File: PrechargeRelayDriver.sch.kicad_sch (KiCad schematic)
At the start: 7 parts, among them K4 G2RL-2A, K7 G7L-2A-X-SI_DC12, Q3 DMN61D8LQ

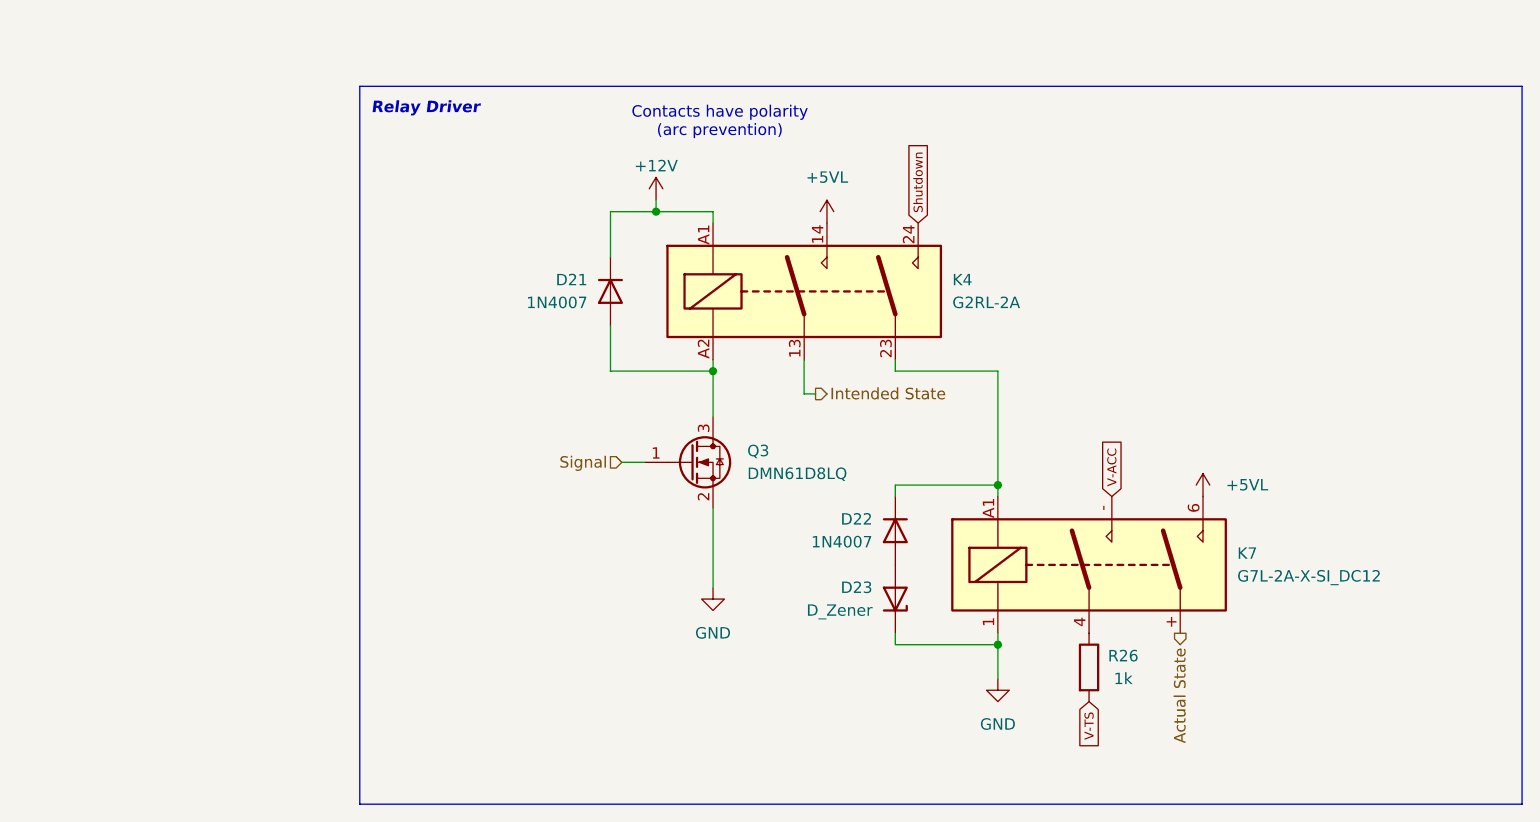
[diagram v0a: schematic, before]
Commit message: Updated to single pole relay, removed relay drivers
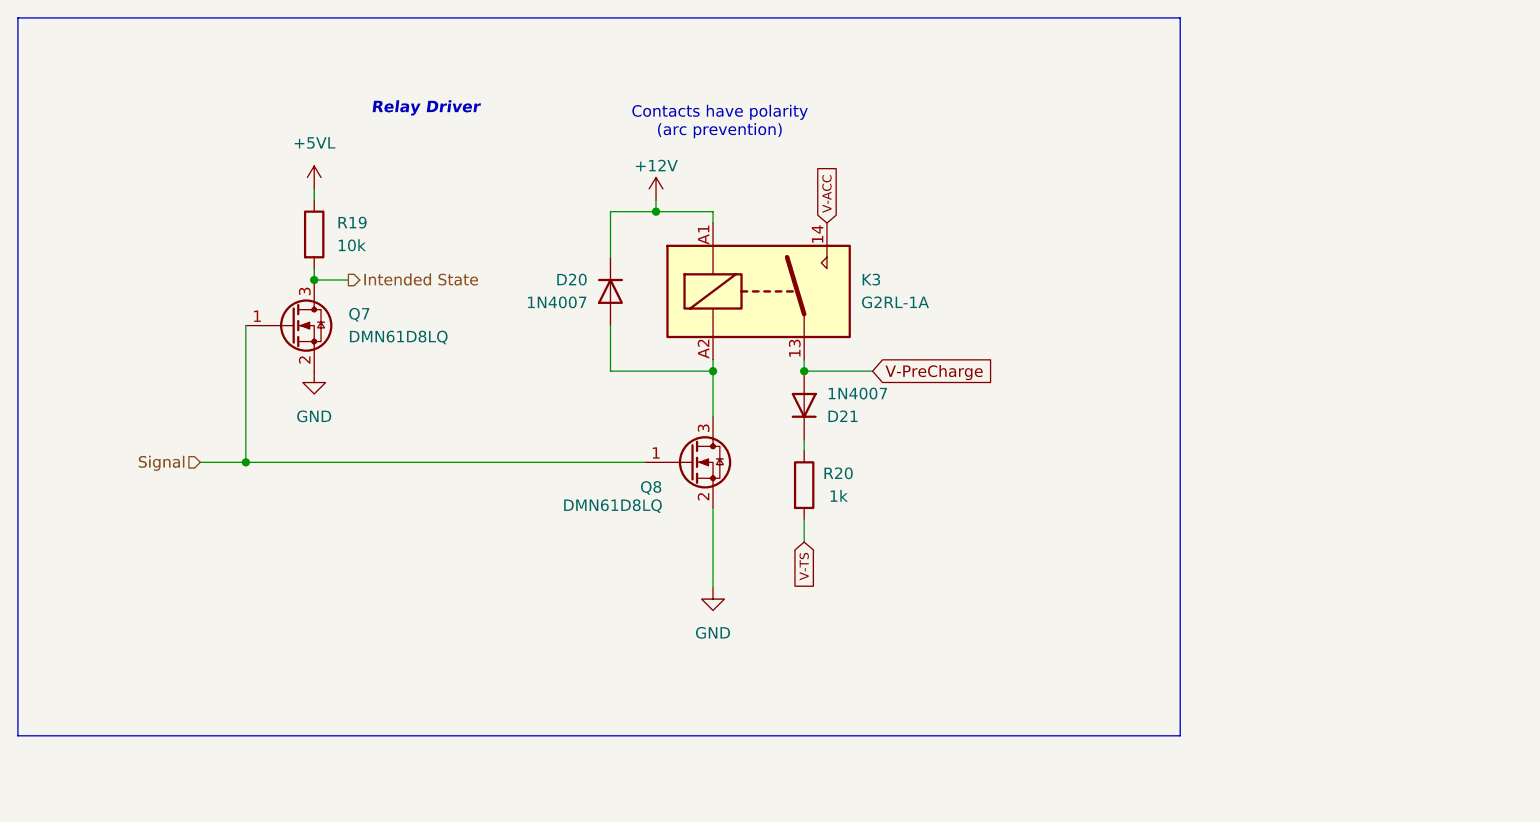
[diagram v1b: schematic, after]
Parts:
- removed D22: 1N4007, Diode_SMD:D_SMA, symbol Diode:1N4007
- removed D23: D_Zener, symbol Device:D_Zener
- removed K4: G2RL-2A, Relay_THT:Relay_DPST_Omron_G2RL-2A, symbol Relay:G2RL-2A
- removed K7: G7L-2A-X-SI_DC12, MyLibrary:G7L2AXSIDC12, symbol Relay:G2RL-2A
- added D21: 1N4007, Diode_SMD:D_SMA, symbol Diode:1N4007
- added K3: G2RL-1A, Relay_THT:Relay_SPST_Omron_G2RL-1A, symbol Relay:G2RL-1A
- added Q7: DMN61D8LQ, Package_TO_SOT_SMD:SOT-23, symbol Transistor_FET:DMN61D8LQ
- added R19: 10k, Resistor_SMD:R_0603_1608Metric, symbol Device:R
- renumbered D21 to D20, Q3 to Q8, R26 to R20
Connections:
- net +12V: now also K3.A1
- net +5VL: now also R19.1
- net GND: now also Q7.2 (S)
- net Intended State: now also Q7.3 (D), R19.2
- net Signal: now also Q7.1 (G)
- net V-ACC: now also K3.14
- net at D20.2 (A), Q8.3 (D): now also K3.A2
- net at R20.1: now also D21.1 (K)
- new net V-PreCharge: D21.2 (A), K3.13
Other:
- moved on the sheet: R20

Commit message: schematic: Cleanup all global labels
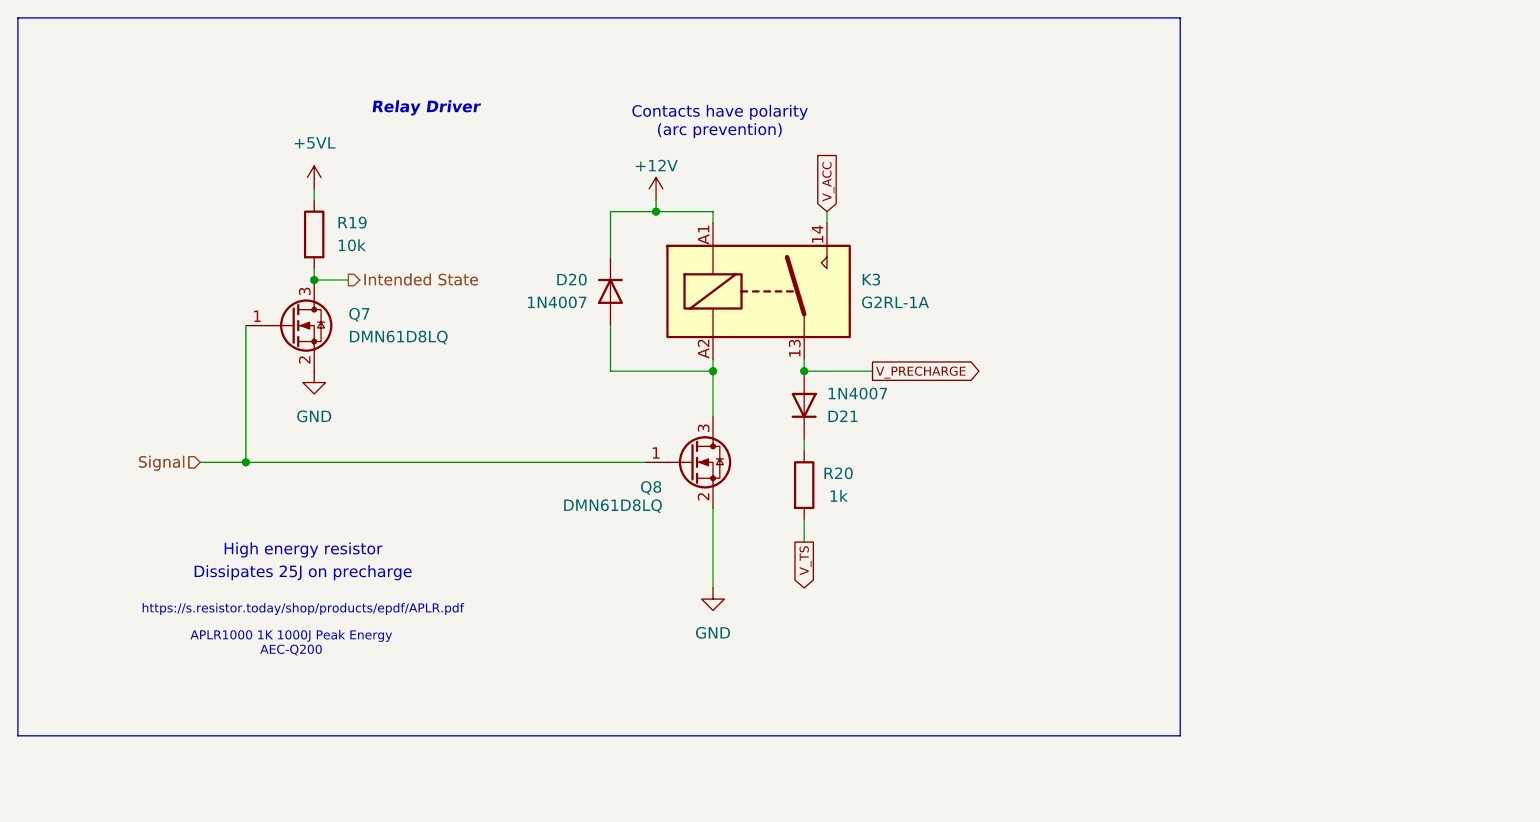
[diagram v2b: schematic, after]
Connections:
- net V-ACC renamed V_ACC
- net V-PreCharge renamed V_PRECHARGE
- net V-TS renamed V_TS
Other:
- note added: "APLR1000 1K 1000J Peak Energy AEC-Q200"
- note added: "Dissipates 25J on precharge"
- note added: "High energy resistor"
- note added: "https://s.resistor.today/shop/products/epdf/APLR.pdf"
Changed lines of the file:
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@@
 		(rev "${REVISION}")
 		(company "York Formula Student")
-		(comment 1 "Designed by Josh B and Logan C")
+		(comment 1 "Designed by Josh B, Logan C, and Owen S")
 	)
 	(rectangle
@@
 		(fill
 			(type none)
+		)
+	)
+	(text "APLR1000 1K 1000J Peak Energy\nAEC-Q200"
+		(exclude_from_sim no)
+		(at 63.5 104.14 0)
+		(effects
+			(font
+				(size 1 1)
+			)
+		)
+	)
+	(text "https://s.resistor.today/shop/products/epdf/APLR.pdf"
+		(exclude_from_sim no)
+		(at 64.77 100.33 0)
+		(effects
+			(font
+				(size 1 1)
+			)
+		)
+	)
+	(text "Dissipates 25J on precharge"
+		(exclude_from_sim no)
+		(at 64.77 96.266 0)
+		(effects
+			(font
+				(size 1.27 1.27)
+			)
+		)
+	)
+	(text "High energy resistor"
+		(exclude_from_sim no)
+		(at 64.77 93.726 0)
+		(effects
+			(font
+				(size 1.27 1.27)
+			)
 		)
 	)
@@
 	(wire
 		(pts
+			(xy 123.19 55.88) (xy 123.19 57.15)
+		)
+		(stroke
+			(width 0)
+			(type default)
+		)
+	)
+	(wire
+		(pts
 			(xy 66.04 53.34) (xy 66.04 54.61)
 		)
@@
 		)
 	)
-	(global_label "V-TS"
-		(shape input)
+	(global_label "V_TS"
+		(shape output)
 		(at 120.65 92.71 270)
 		(fields_autoplaced yes)
@@
 		)
 		(property "Intersheetrefs" "${INTERSHEET_REFS}"
-			(at 120.65 98.8698 90)
+			(at 120.65 98.3936 90)
 			(effects
 				(font
@@
 		)
 	)
-	(global_label "V-PreCharge"
-		(shape input)
+	(global_label "V_PRECHARGE"
+		(shape output)
 		(at 128.27 73.66 0)
 		(fields_autoplaced yes)
 		(effects
 			(font
-				(size 1.27 1.27)
+				(size 1 1)
 			)
 			(justify left)
 		)
 		(property "Intersheetrefs" "${INTERSHEET_REFS}"
-			(at 143.6528 73.66 0)
+			(at 140.9536 73.66 0)
 			(effects
 				(font
@@
 		)
 	)
-	(global_label "V-ACC"
+	(global_label "V_ACC"
 		(shape input)
-		(at 123.19 57.15 90)
+		(at 123.19 55.88 90)
 		(fields_autoplaced yes)
 		(effects
@@
 		)
 		(property "Intersheetrefs" "${INTERSHEET_REFS}"
-			(at 123.19 49.8474 90)
+			(at 123.19 49.0536 90)
 			(effects
 				(font
